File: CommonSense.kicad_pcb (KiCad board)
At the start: 2 copper layers, 35 x 24 mm, 37 parts, among them J1 Conn_02x04_Counter_Clockwise, J2 Conn_01x02, J3 Conn_01x02, J5 Conn_ARM_SWD_TagConnect_TC203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, U1 NRF52810-QFAA-R7, U2 SHT41-AD1B-R2, Y1 ECS-.327-12.5-12R-TR, Y2 ABM11W-32.0000MHZ-7-D1X-T3

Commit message: Changed Antenna icon to chip antenna and fixed designator
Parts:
- removed 2108838-1: ~, encyclopedia_galactica:2108838-1
- added AE1: 2108838-1, encyclopedia_galactica:2108838-1, F.Cu at (135.7, 68.0)
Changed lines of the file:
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@@
   (net 49 "+BATT")
   (net 50 "+3V0")
+  (net 51 "unconnected-(AE1-PCB_Trace-Pad2)")
   (footprint "Diode_SMD:D_0603_1608Metric" (layer "F.Cu")
     (at 152.1 57 180)
@@
     (pad "2" smd rect (at 0.7 0 180) (size 0.6 1.1) (layers "F.Cu" "F.Paste" "F.Mask")
       (net 3 "/XL1") (pinfunction "2") (pintype "passive"))
-  )
-  (footprint "encyclopedia_galactica:2108838-1" (layer "F.Cu")
-    (at 135.7 68)
-    (property "Sheetfile" "CommonSense.kicad_sch")
-    (property "Sheetname" "")
-    (property "ki_description" "Antenna")
-    (property "ki_keywords" "antenna")
-    (attr smd)
-    (fp_text reference "2108838-1" (at 0 -11 unlocked) (layer "F.SilkS") hide
-        (effects (font (size 1 1) (thickness 0.1)))
-    )
-    (fp_text value "~" (at 0 -9.5 unlocked) (layer "F.Fab") hide
-        (effects (font (size 1 1) (thickness 0.15)))
-    )
-    (fp_text user "${REFERENCE}" (at 0 -8 unlocked) (layer "F.Fab") hide
-        (effects (font (size 1 1) (thickness 0.15)))
-    )
-    (fp_line (start -6.5 -5) (end 6.5 -5)
-      (stroke (width 0.1) (type default)) (layer "F.CrtYd"))
-    (fp_line (start -6.5 5) (end -6.5 -5)
-      (stroke (width 0.1) (type default)) (layer "F.CrtYd"))
-    (fp_line (start 6.5 -5) (end 6.5 5)
-      (stroke (width 0.1) (type default)) (layer "F.CrtYd"))
-    (fp_line (start 6.5 5) (end -6.5 5)
-      (stroke (width 0.1) (type default)) (layer "F.CrtYd"))
-    (pad "1" smd rect (at 4.1 0) (size 0.8 1.8) (layers "F.Cu" "F.Paste" "F.Mask")
-      (net 1 "/RF") (pinfunction "A") (pintype "input") (thermal_bridge_angle 45))
-    (pad "2" smd rect (at 0.9 0) (size 0.8 1.8) (layers "F.Cu" "F.Paste" "F.Mask")
-      (thermal_bridge_angle 45))
-    (zone (net 0) (net_name "") (layers "*.Cu") (hatch edge 0.5)
-      (connect_pads (clearance 0))
-      (min_thickness 0.25) (filled_areas_thickness no)
-      (keepout (tracks allowed) (vias not_allowed) (pads allowed) (copperpour not_allowed) (footprints not_allowed))
-      (fill (thermal_gap 0.5) (thermal_bridge_width 0.5))
-      (polygon
-        (pts
-          (xy 129.2 63)
-          (xy 129.2 73)
-          (xy 142.2 73)
-          (xy 142.2 63)
-        )
-      )
-    )
   )
   (footprint "MountingHole:MountingHole_2.2mm_M2" locked (layer "F.Cu")
@@
     )
   )
+  (footprint "encyclopedia_galactica:2108838-1" locked (layer "F.Cu")
+    (at 135.7 68)
+    (property "Sheetfile" "CommonSense.kicad_sch")
+    (property "Sheetname" "")
+    (property "ki_description" "Ceramic chip antenna with pin for PCB trace")
+    (property "ki_keywords" "antenna")
+    (attr smd)
+    (fp_text reference "AE1" (at 0 -11 unlocked) (layer "F.SilkS") hide
+        (effects (font (size 1 1) (thickness 0.1)))
+    )
+    (fp_text value "2108838-1" (at 0 -9.5 unlocked) (layer "F.Fab") hide
+        (effects (font (size 1 1) (thickness 0.15)))
+    )
+    (fp_text user "${REFERENCE}" (at 0 -8 unlocked) (layer "F.Fab") hide
+        (effects (font (size 1 1) (thickness 0.15)))
+    )
+    (fp_line (start -6.5 -5) (end 6.5 -5)
+      (stroke (width 0.1) (type default)) (layer "F.CrtYd"))
+    (fp_line (start -6.5 5) (end -6.5 -5)
+      (stroke (width 0.1) (type default)) (layer "F.CrtYd"))
+    (fp_line (start 6.5 -5) (end 6.5 5)
+      (stroke (width 0.1) (type default)) (layer "F.CrtYd"))
+    (fp_line (start 6.5 5) (end -6.5 5)
+      (stroke (width 0.1) (type default)) (layer "F.CrtYd"))
+    (pad "1" smd rect locked (at 4.1 0) (size 0.8 1.8) (layers "F.Cu" "F.Paste" "F.Mask")
+      (net 1 "/RF") (pinfunction "FEED") (pintype "input") (thermal_bridge_angle 45))
+    (pad "2" smd rect locked (at 0.9 0) (size 0.8 1.8) (layers "F.Cu" "F.Paste" "F.Mask")
+      (net 51 "unconnected-(AE1-PCB_Trace-Pad2)") (pinfunction "PCB_Trace") (pintype "passive+no_connect") (thermal_bridge_angle 45))
+    (zone (net 0) (net_name "") (layers "*.Cu") (hatch edge 0.5)
+      (connect_pads (clearance 0))
+      (min_thickness 0.25) (filled_areas_thickness no)
+      (keepout (tracks allowed) (vias not_allowed) (pads allowed) (copperpour not_allowed) (footprints not_allowed))
+      (fill (thermal_gap 0.5) (thermal_bridge_width 0.5))
+      (polygon
+        (pts
+          (xy 129.2 63)
+          (xy 129.2 73)
+          (xy 142.2 73)
+          (xy 142.2 63)
+        )
+      )
+    )
+  )

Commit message: Change battery holder value to component number
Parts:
- BT1: value Battery_Cell -> 3034
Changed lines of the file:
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@@
         (effects (font (size 1 1) (thickness 0.15)) (justify mirror))
     )
-    (fp_text value "Battery_Cell" (at 0 -11.5 90) (layer "B.Fab") hide
+    (fp_text value "3034" (at 0 -11.5 90) (layer "B.Fab") hide
         (effects (font (size 1 1) (thickness 0.15)) (justify mirror))
     )

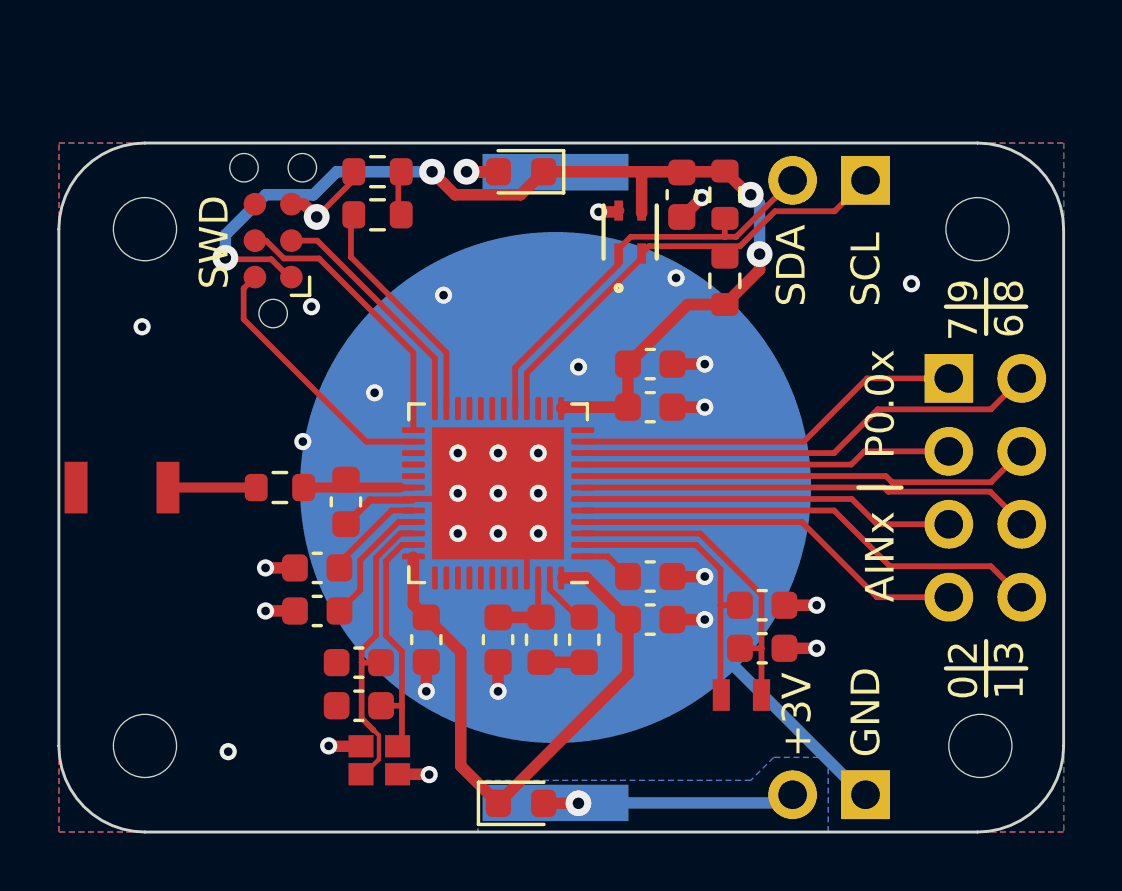
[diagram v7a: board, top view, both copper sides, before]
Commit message: Move I2C pullups closer to nrf chip; Moved I2C lines further appart
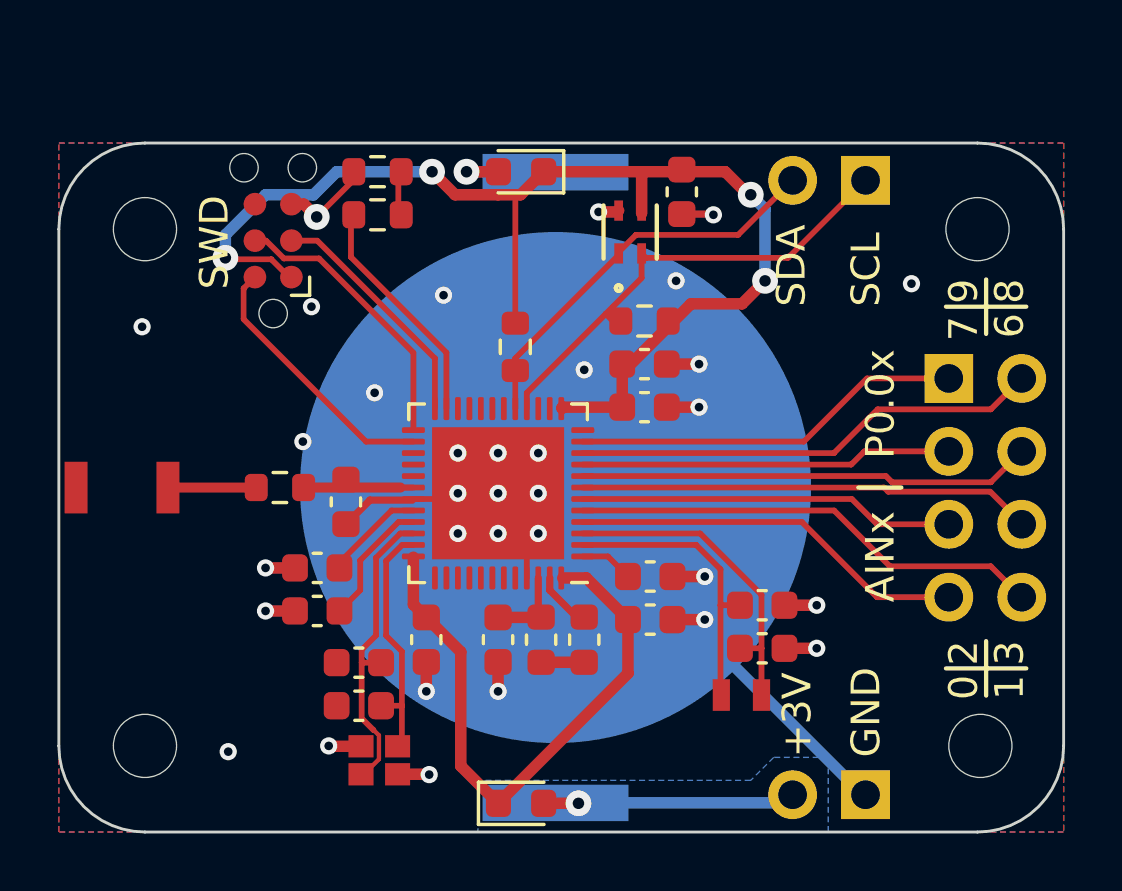
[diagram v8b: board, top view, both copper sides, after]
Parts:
- moved R4 9.02 mm to (151.9, 63.1)
- moved R3 3.13 mm to (156.4, 62.2), turned to 0 degrees
- moved C14 0.20 mm to (156.4, 63.7)
- moved C4 0.20 mm to (156.4, 65.2)
- moved C13 0.10 mm to (157.7, 57.7)
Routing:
- net +3V0: track 58.5 -> 63.3 mm
- net /SCL: track 15.9 -> 16.7 mm
- net /SDA: track 14.7 -> 14.0 mm
